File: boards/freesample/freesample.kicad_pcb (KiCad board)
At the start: 8 copper layers, 576 parts, among them J1 SMA, J10 XILINX_JTAG, J11 SMA, J12 SMA, J13 SMA, J14 SMA, J15 SMA, J16 SMA, J17 SMA, J18 SMA, J19 JUMPER, J2 BARREL, J20 JUMPER, J21 JUMPER, J22 SMA, J23 SMA, J24 SMA, J25 SMA, J26 PMOD_HOST, J3 SMA, J4 SMA, J5 SMA, J6 XILINX_JTAG, J7 CONN_INTEGRALSTICK_FPGA_HOST, J8 CONN_INTEGRALSTICK_MCU_HOST, J9 0826-1G1T-23-F, M1 TRACEPAD, M2 LOGO1, M3 LOGO2, M4 LOGO3, M5 LOGO4, M6 LOGO5, M7 LOGO6, Q1 SSM6N58NU, U1 HMC675LP3E, U10 PI6C59S6005, U11 PI6C59S6005, U12 PI6C59S6005, U13 SIP32408, U14 LMK04806, U15 ASG-D-V-A-125.000MHZ, U16 HMC856, U17 NB6L295, U18 PI6C59S6005, U19 NB7V52MMNG, U2 HMC675LP3E, U20 NB7V52MMNG, U21 NB7V52MMNG, U22 PI6C59S6005, U26 MCP1755ST-5002E/MC, U27 LM27761, U28 ADP1763Z-1.0, U29 ADP1763Z-1.0, U3 PI6C59S6005, U30 OKL-T/3-W12P-C, U31 ADP1741, U32 OKL-T/3-W12P-C, U33 ADP1741, U34 ADP1741, U35 OKL-T/3-W12P-C, U36 OKL-T/3-W12P-C, U37 LM27761, U38 OKL-T/3-W12P-C, U39 LM27761, U4 LTC2664CUH-16#PBF, U40 DS25BR150, U41 DS25BR150, U42 ADP1741, U43 ADP1741, U5 TLK10232, U6 LMK61PD0A2, U7 PI6C59S6005, U8 HMC675LP3E, U9 HMC675LP3E

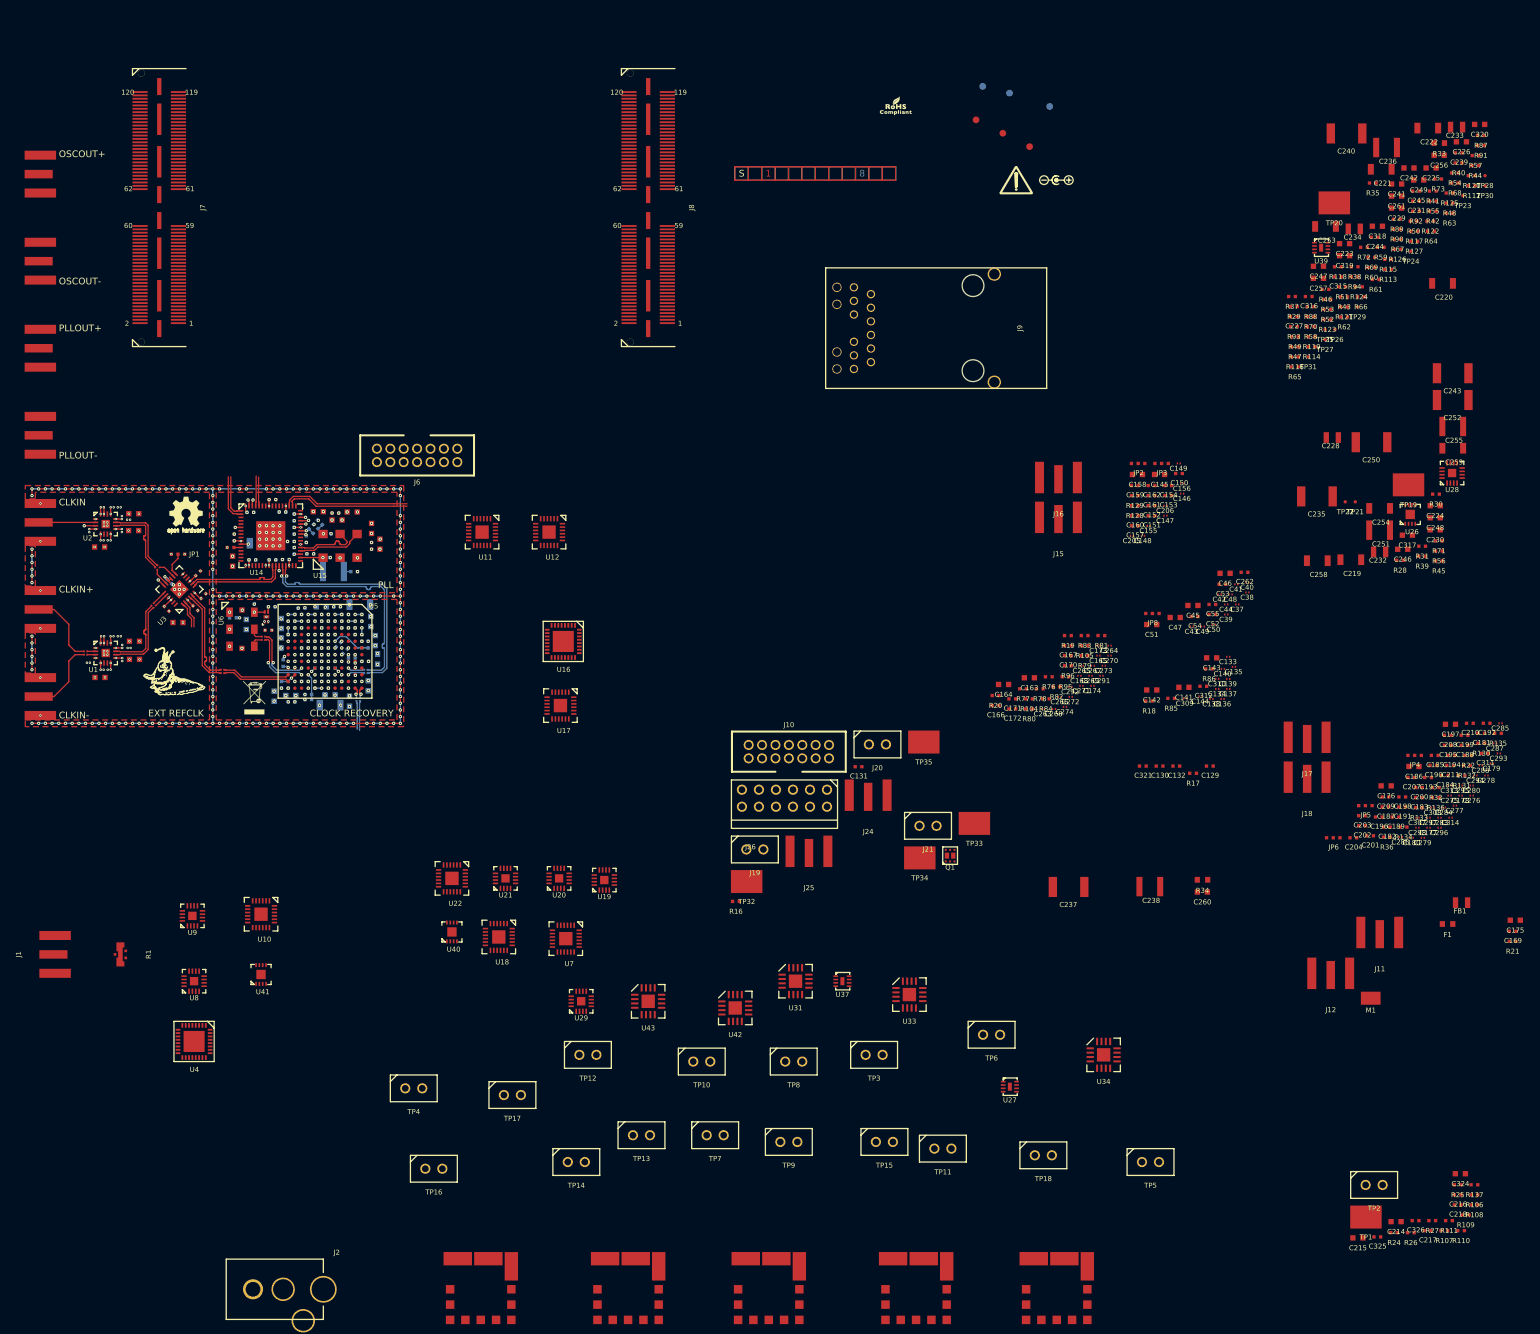
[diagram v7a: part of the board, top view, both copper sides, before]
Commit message: Tweaks to PLL and CDR layout, swapped a few signals around. Began work on level trigger and ADC layout.
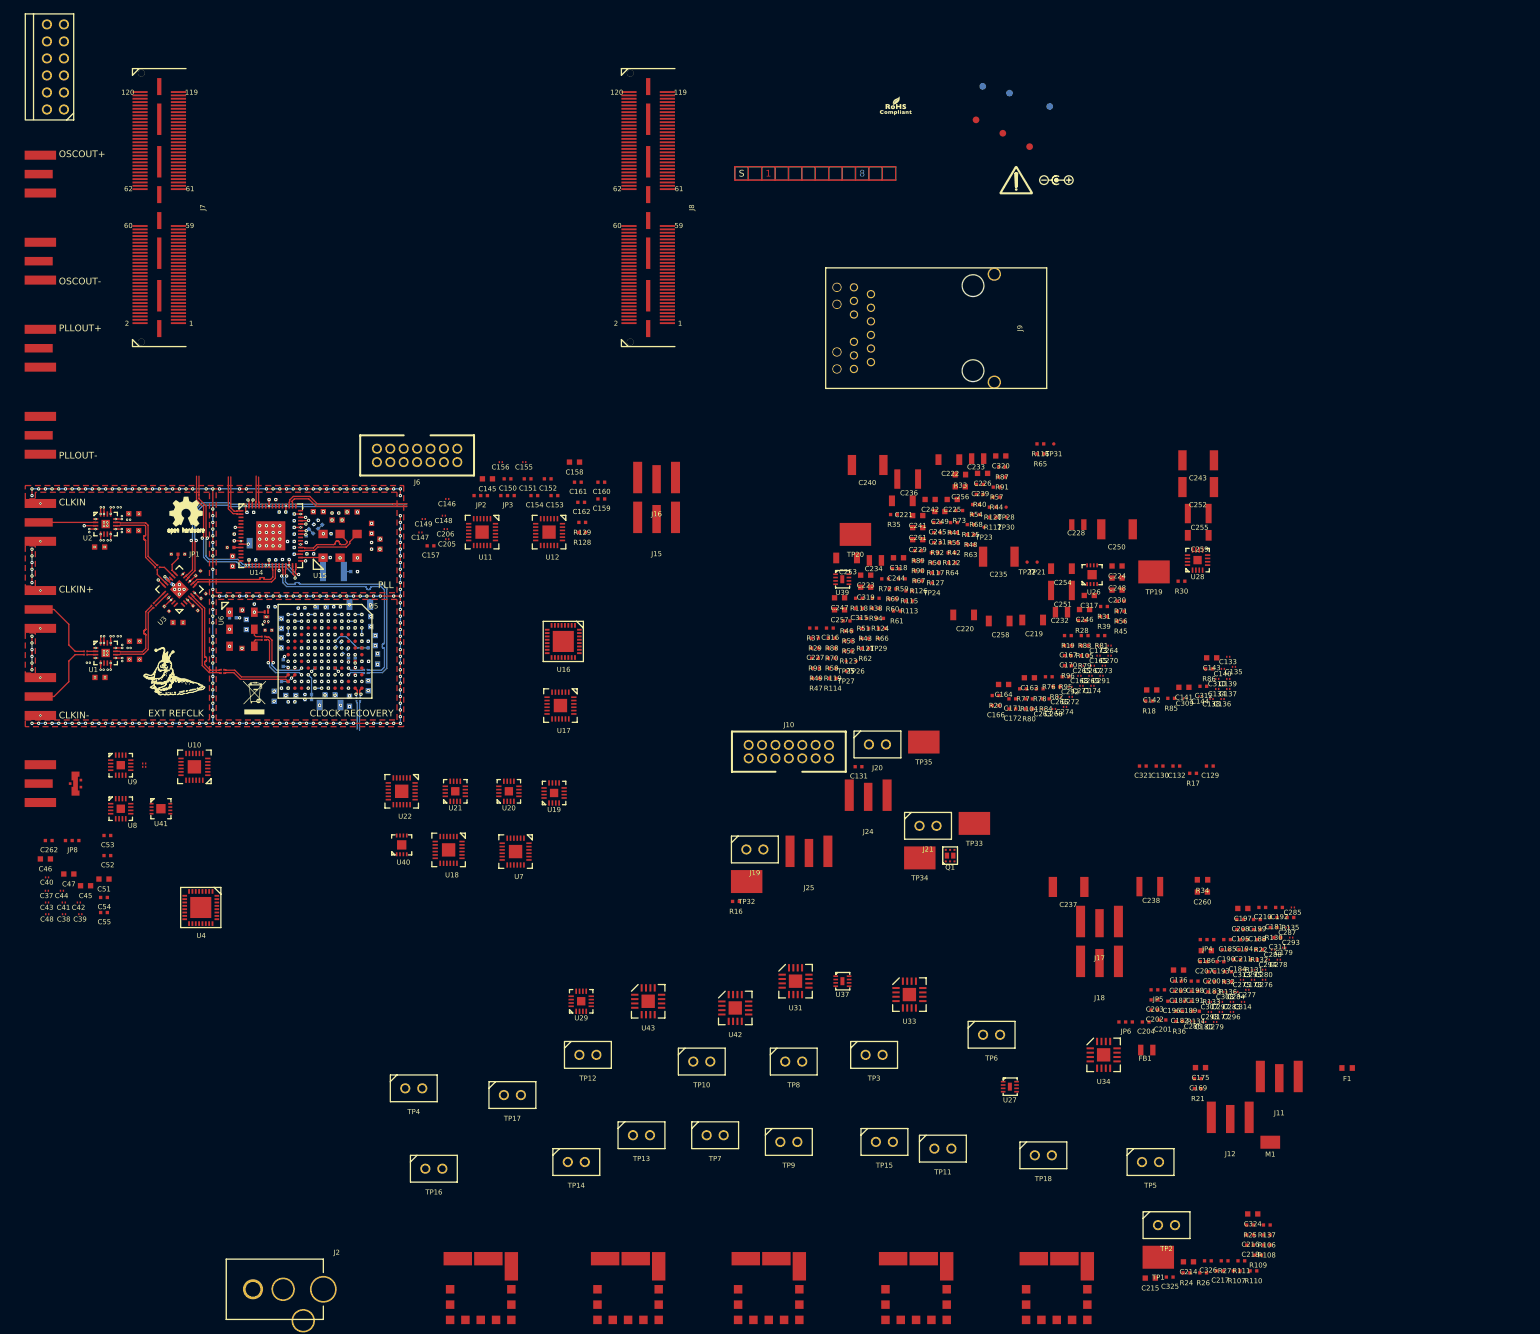
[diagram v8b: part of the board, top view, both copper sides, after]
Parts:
- moved C40 184.5 mm to (19.2, 178.0)
- moved C38 183.1 mm to (21.8, 183.5)
- moved C48 183.0 mm to (19.3, 183.5)
- moved C262 183.0 mm to (19.5, 172.5)
- moved C37 182.8 mm to (19.2, 180.0)
- moved C41 181.4 mm to (21.8, 181.8)
- moved C46 181.2 mm to (19.0, 175.2)
- moved C44 179.0 mm to (21.5, 180.0)
- moved C39 176.8 mm to (24.2, 183.5)
- moved C42 176.4 mm to (24.0, 181.8)
- moved C43 175.8 mm to (19.2, 181.8)
- moved C55 171.8 mm to (27.8, 183.2)
- moved C53 170.7 mm to (28.2, 171.8)
- moved C45 170.5 mm to (25.0, 179.2)
- moved C47 169.6 mm to (22.5, 177.5)
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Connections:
- net Net-(C49-Pad2) renamed /Level triggering/LTRIG_P
- net Net-(C50-Pad2) renamed /Level triggering/LTRIG_N
- C49 pad 1: Net-(C49-Pad1) -> /Level triggering/LTRIG_AC_P
- C50 pad 1: Net-(C50-Pad1) -> /Level triggering/LTRIG_AC_N
- R1 pad 2: /VIN_0 -> /ADC_DIN
- R1 pad 3: /VIN_1 -> /LTRIG_DIN
- U10 pad 1: /CDR/CDR_DIN_P -> /CDR/CDR_DIN_N
- U10 pad 14: Net-(C50-Pad1) -> /Level triggering/LTRIG_AC_P
- U10 pad 17: Net-(C49-Pad1) -> /Level triggering/LTRIG_AC_N
- U10 pad 2: /CDR/CDR_DIN_N -> /CDR/CDR_DIN_P
- U10 pad 23: /Level triggering/LTRIG_SAMPOUT_P -> /Level triggering/LTRIG_SAMPOUT_N
- U10 pad 24: /Level triggering/LTRIG_SAMPOUT_N -> /Level triggering/LTRIG_SAMPOUT_P
- U3 pad 1: /Sample clock muxing/EXT_SAMPCLK_N -> (no net)
- U3 pad 10: (no net) -> /Sample clock muxing/EXT_SAMPCLK_N
- U3 pad 11: (no net) -> /Sample clock muxing/EXT_SAMPCLK_P
- U3 pad 2: /Sample clock muxing/EXT_SAMPCLK_P -> (no net)
- U8 pad 2: /VIN_1 -> /ADC_DIN
- U9 pad 2: /VIN_0 -> /LTRIG_DIN
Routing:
- net /Sample clock muxing/EXT_SAMPCLK_P: track 4.19 -> 42.9 mm, vias 0 -> 1
- net /Sample clock muxing/EXT_SAMPCLK_N: track 3.89 -> 42.6 mm, vias 0 -> 1
- net /PLL/OSCOUT_P: track 0.00 -> 29.8 mm, vias 0 -> 2
- net /PLL/OSCOUT_N: track 0.00 -> 29.2 mm, vias 0 -> 2
- net /PLL_LD: track 0.00 -> 14.7 mm, vias 0 -> 1
- net /3V3_PLL: track 93.6 -> 99.5 mm
- net /CDR/SERDES_TMS: track 29.3 -> 27.2 mm
- net /CDR/SERDES_TDI: track 29.5 -> 28.7 mm
- net /CDR/SERDES_TDO: track 21.1 -> 20.4 mm
- net /GND: vias 373 -> 369
